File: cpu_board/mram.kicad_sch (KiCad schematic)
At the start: 8 parts, among them U3 EM064LXQADG13IS1T

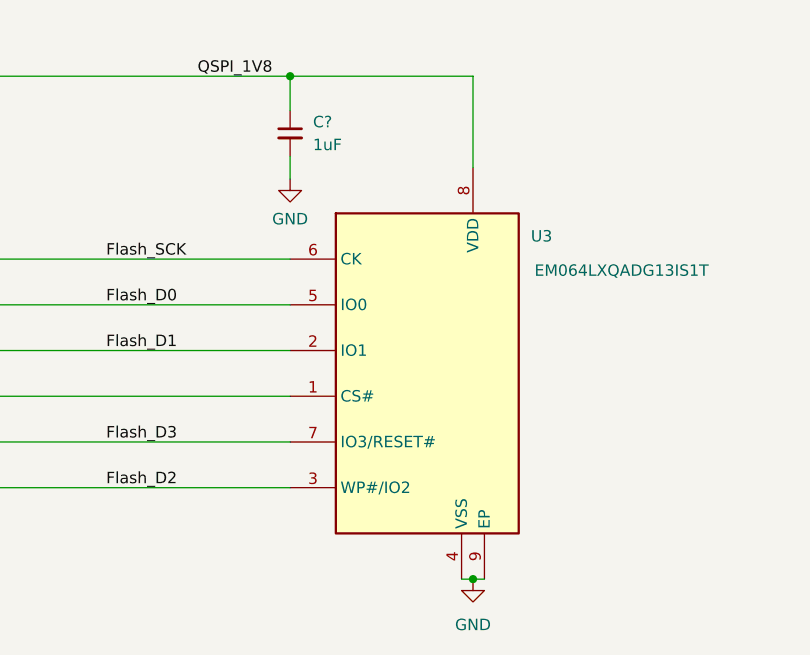
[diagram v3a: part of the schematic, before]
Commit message: clean up silkscreen
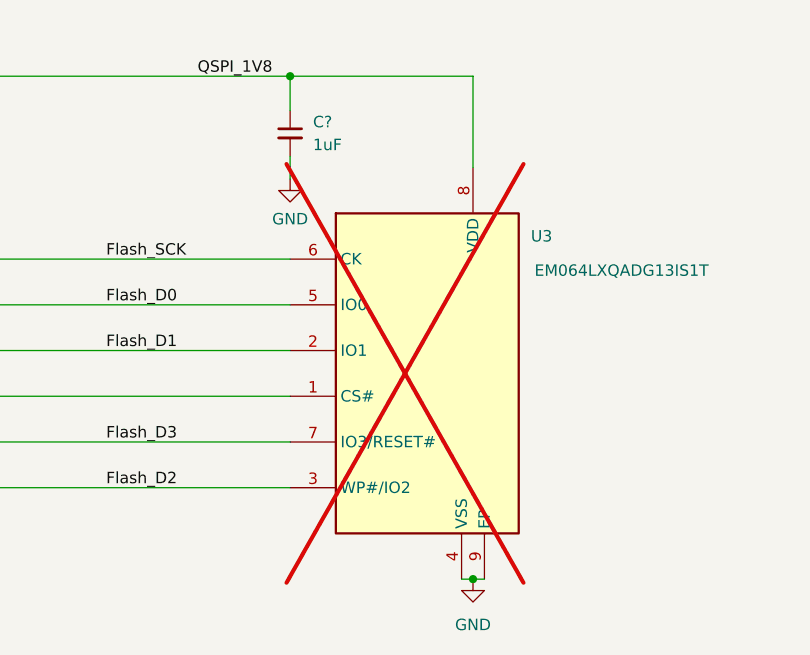
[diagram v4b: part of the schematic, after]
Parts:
- U3: now not fitted
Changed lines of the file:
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@@
       (effects (font (size 1.27 1.27)) hide)
     )
-    (property "Datasheet" "~" (at 199.39 90.17 0)
+    (property "Datasheet" "" (at 199.39 90.17 0)
       (effects (font (size 1.27 1.27)) hide)
     )
@@
   )
   (symbol (lib_id "adcs:EM064LXQADG13IS1T") (at 234.315 213.36 0) (unit 1)
-    (in_bom yes) (on_board yes) (dnp no)
+    (in_bom yes) (on_board yes) (dnp yes)
     (property "Reference" "U3" (at 262.255 199.39 0)
       (effects (font (size 1.27 1.27)))
@@
     (property "Footprint (for JLCPCB)" "" (at 234.315 213.36 0)
       (effects (font (size 1.27 1.27)) hide)
+    )
+    (property "DigiKey Part Number" "" (at 234.315 213.36 0)
+      (effects (font (size 1.27 1.27)) hide)
+    )
+    (property "Tolerance" "" (at 234.315 213.36 0)
+      (effects (font (size 1.27 1.27)))
+    )
+    (property "Power Rating" "" (at 234.315 213.36 0)
+      (effects (font (size 1.27 1.27)))
     )
     (pin "1")
@@
       (effects (font (size 1.27 1.27)) hide)
     )
-    (property "Datasheet" "~" (at 208.28 90.17 0)
-      (effects (font (size 1.27 1.27)) hide)
-    )
+    (property "Datasheet" "" (at 208.28 90.17 0)
+      (effects (font (size 1.27 1.27)) hide)
+    )

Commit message: soldermander 1.0 ready for review
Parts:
- C? (x2): Voltage Rating (none) -> 50V
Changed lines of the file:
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@@
       (effects (font (size 1.27 1.27)))
+    )
+    (property "Voltage Rating" "50V" (at 234.315 86.36 0)
+      (effects (font (size 1.27 1.27)) hide)
     )
     (pin "1")
@@
       (effects (font (size 1.27 1.27)))
     )
+    (property "Voltage Rating" "50V" (at 234.315 187.96 0)
+      (effects (font (size 1.27 1.27)) hide)
+    )
     (pin "1")

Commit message: update
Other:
- company: (none) -> Stanford Student Space Initiative
- title: (none) -> Soldermander
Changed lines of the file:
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@@
 (kicad_sch (version 20230121) (generator eeschema)
   (paper "A3")
+  (title_block
+    (title "Soldermander")
+    (date "2024-02-27")
+    (rev "1.0")
+    (company "Stanford Student Space Initiative")
+    (comment 1 "RE: Flynn Dreilinger")
+  )
   (junction (at 199.39 120.65) (diameter 0) (color 0 0 0 0)
   )
